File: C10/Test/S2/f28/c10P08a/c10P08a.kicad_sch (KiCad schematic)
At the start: 5 parts

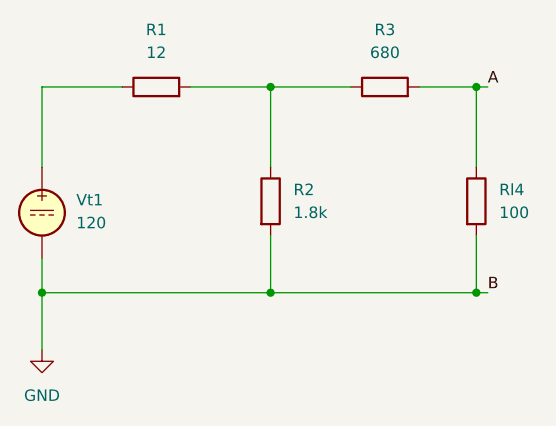
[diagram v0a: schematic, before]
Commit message: corrected from misprinting Fig 10-28
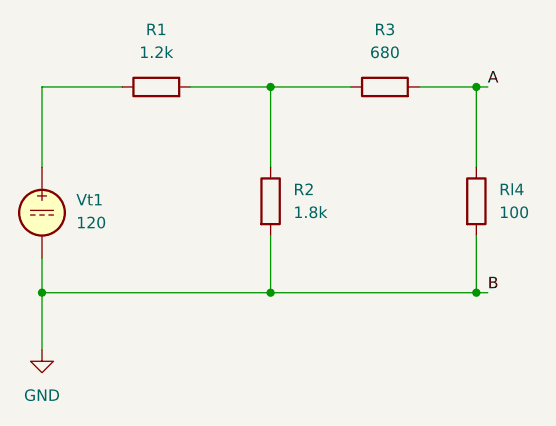
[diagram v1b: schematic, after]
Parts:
- R1: value 12 -> 1.2k
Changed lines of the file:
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@@
 			)
 		)
-		(property "Value" "12"
+		(property "Value" "1.2k"
 			(at 148.59 66.04 90)
 			(show_name no)
